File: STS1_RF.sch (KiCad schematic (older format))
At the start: 6 parts

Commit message: finished schematic
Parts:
- C13, C14, C15, C16: renamed from C?; footprint (none) -> Capacitor_SMD:C_0805_2012Metric
- gave numbers to parts that had none: 2
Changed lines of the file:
@@
 $EndDescr
 $Comp
-L STS1_COBC_RFM:LoRa126XF30 RF?
+L STS1_COBC_RFM:LoRa126XF30 RF1
 U 1 1 612D3FCA
 P 3850 3450
-F 0 "RF?" H 3850 4025 50  0000 C CNN
+F 0 "RF1" H 3850 4025 50  0000 C CNN
 F 1 "LoRa1268F30" H 3850 3934 50  0000 C CNN
 F 2 "" H 3850 3900 50  0001 C CNN
@@
 $EndComp
 $Comp
-L STS1_COBC_RFM:RF4463F30 RF?
+L STS1_COBC_RFM:RF4463F30 RF2
 U 1 1 612D4F50
 P 8200 3600
-F 0 "RF?" H 8200 4225 50  0000 C CNN
+F 0 "RF2" H 8200 4225 50  0000 C CNN
 F 1 "RF4463F30" H 8200 4134 50  0000 C CNN
 F 2 "" H 8200 4100 50  0001 C CNN
@@
 LoRa_VCC
 $Comp
-L power:GND #PWR?
+L power:GND #PWR0147
 U 1 1 612D692F
 P 3300 3200
-F 0 "#PWR?" H 3300 2950 50  0001 C CNN
+F 0 "#PWR0147" H 3300 2950 50  0001 C CNN
 F 1 "GND" V 3305 3072 50  0000 R CNN
 F 2 "" H 3300 3200 50  0001 C CNN
@@
 $EndComp
 $Comp
-L power:GND #PWR?
+L power:GND #PWR0148
 U 1 1 612D703E
 P 3300 3800
-F 0 "#PWR?" H 3300 3550 50  0001 C CNN
+F 0 "#PWR0148" H 3300 3550 50  0001 C CNN
 F 1 "GND" V 3305 3672 50  0000 R CNN
 F 2 "" H 3300 3800 50  0001 C CNN
@@
 	2550 3100 2650 3100
 $Comp
-L Device:C C?
+L Device:C C14
 U 1 1 612D80B3
 P 2900 3350
-F 0 "C?" H 3015 3396 50  0000 L CNN
+F 0 "C14" H 3015 3396 50  0000 L CNN
 F 1 "47u" H 3015 3305 50  0000 L CNN
-F 2 "" H 2938 3200 50  0001 C CNN
+F 2 "Capacitor_SMD:C_0805_2012Metric" H 2938 3200 50  0001 C CNN
 F 3 "~" H 2900 3350 50  0001 C CNN
 	1    2900 3350
@@
 $EndComp
 $Comp
-L Device:C C?
+L Device:C C13
 U 1 1 612D8225
 P 2650 3350
-F 0 "C?" H 2450 3450 50  0000 L CNN
+F 0 "C13" H 2450 3450 50  0000 L CNN
 F 1 "100n" H 2500 3350 50  0000 L CNN
-F 2 "" H 2688 3200 50  0001 C CNN
+F 2 "Capacitor_SMD:C_0805_2012Metric" H 2688 3200 50  0001 C CNN
 F 3 "~" H 2650 3350 50  0001 C CNN
 	1    2650 3350
@@
 $EndComp
 $Comp
-L power:GND #PWR?
+L power:GND #PWR0149
 U 1 1 612D8F9E
 P 2650 3500
-F 0 "#PWR?" H 2650 3250 50  0001 C CNN
+F 0 "#PWR0149" H 2650 3250 50  0001 C CNN
 F 1 "GND" H 2655 3327 50  0000 C CNN
 F 2 "" H 2650 3500 50  0001 C CNN
@@
 $EndComp
 $Comp
-L power:GND #PWR?
+L power:GND #PWR0150
 U 1 1 612D9513
 P 2900 3500
-F 0 "#PWR?" H 2900 3250 50  0001 C CNN
+F 0 "#PWR0150" H 2900 3250 50  0001 C CNN
 F 1 "GND" H 2905 3327 50  0000 C CNN
 F 2 "" H 2900 3500 50  0001 C CNN
@@
 	2900 3100 3300 3100
 $Comp
-L power:GND #PWR?
+L power:GND #PWR0151
 U 1 1 612D987F
 P 3300 3500
-F 0 "#PWR?" H 3300 3250 50  0001 C CNN
+F 0 "#PWR0151" H 3300 3250 50  0001 C CNN
 F 1 "GND" V 3305 3372 50  0000 R CNN
 F 2 "" H 3300 3500 50  0001 C CNN
@@
 RF4463_VCC
 $Comp
-L power:GND #PWR?
+L power:GND #PWR0152
 U 1 1 612DA405
 P 7650 3300
-F 0 "#PWR?" H 7650 3050 50  0001 C CNN
+F 0 "#PWR0152" H 7650 3050 50  0001 C CNN
 F 1 "GND" V 7655 3172 50  0000 R CNN
 F 2 "" H 7650 3300 50  0001 C CNN
@@
 $EndComp
 $Comp
-L power:GND #PWR?
+L power:GND #PWR0153
 U 1 1 612DA9D3
 P 7650 3600
-F 0 "#PWR?" H 7650 3350 50  0001 C CNN
+F 0 "#PWR0153" H 7650 3350 50  0001 C CNN
 F 1 "GND" V 7655 3472 50  0000 R CNN
 F 2 "" H 7650 3600 50  0001 C CNN
@@
 $EndComp
 $Comp
-L power:GND #PWR?
+L power:GND #PWR0154
 U 1 1 612DAECB
 P 7650 3900
-F 0 "#PWR?" H 7650 3650 50  0001 C CNN
+F 0 "#PWR0154" H 7650 3650 50  0001 C CNN
 F 1 "GND" V 7655 3772 50  0000 R CNN
 F 2 "" H 7650 3900 50  0001 C CNN
@@
 RF4463_ANT
 $Comp
-L Device:C C?
+L Device:C C16
 U 1 1 612DB4E1
 P 7250 3350
-F 0 "C?" H 7200 3350 50  0000 L CNN
+F 0 "C16" H 7200 3350 50  0000 L CNN
 F 1 "47u" H 7200 3250 50  0000 L CNN
-F 2 "" H 7288 3200 50  0001 C CNN
+F 2 "Capacitor_SMD:C_0805_2012Metric" H 7288 3200 50  0001 C CNN
 F 3 "~" H 7250 3350 50  0001 C CNN
 	1    7250 3350
@@
 	7250 3200 7650 3200
 $Comp
-L Device:C C?
+L Device:C C15
 U 1 1 612DBAA7
 P 7000 3350
-F 0 "C?" H 6900 3350 50  0000 L CNN
+F 0 "C15" H 6900 3350 50  0000 L CNN
 F 1 "100n" H 6950 3250 50  0000 L CNN
-F 2 "" H 7038 3200 50  0001 C CNN
+F 2 "Capacitor_SMD:C_0805_2012Metric" H 7038 3200 50  0001 C CNN
 F 3 "~" H 7000 3350 50  0001 C CNN
 	1    7000 3350
@@
 $EndComp
 $Comp
-L power:GND #PWR?
+L power:GND #PWR0155
 U 1 1 612DBF97
 P 7000 3500
-F 0 "#PWR?" H 7000 3250 50  0001 C CNN
+F 0 "#PWR0155" H 7000 3250 50  0001 C CNN
 F 1 "GND" H 7005 3327 50  0000 C CNN
 F 2 "" H 7000 3500 50  0001 C CNN
@@
 $EndComp
 $Comp
-L power:GND #PWR?
+L power:GND #PWR0156
 U 1 1 612DC2BC
 P 7250 3500
-F 0 "#PWR?" H 7250 3250 50  0001 C CNN
+F 0 "#PWR0156" H 7250 3250 50  0001 C CNN
 F 1 "GND" H 7255 3327 50  0000 C CNN
 F 2 "" H 7250 3500 50  0001 C CNN

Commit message: schematic done
final tweaks (adding LEDS, pin headers, moving circuits...)
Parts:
- added D5: LED, symbol Device:LED
- added J39, J40: Conn_Coaxial, symbol Connector:Conn_Coaxial
- added JP3, JP4, JP? (x2): Jumper_NC_Dual, symbol Device:Jumper_NC_Dual
- added R13: 15, symbol Device:R
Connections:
- net GND: now also JP3.1, JP4.1, JP?.3, JP?.3, R13.2; no longer RF1.5 (NRESET), RF2.5 (SDN)
- net LoRa_SMA_GND: now also J39.2 (Ext)
- net LoRa_VCC: now also JP3.3, JP?.1, JP?.1
- net RF4463_ANT_GND: now also J40.2 (Ext)
- net RF4463_VCC: now also JP4.3
- net at RF1.13 (DIO1): now also JP?.2
- net at RF1.14 (DIO3): now also JP?.2
- net at RF1.6 (BUSY): now also D5.2 (A)
- net LoRa_ANT: no longer names the net of RF1.16 (ANT)
- net LoRa_ANT: now also J39.1 (In)
- net RF4463_ANT: no longer names the net of RF2.16 (ANT)
- net RF4463_ANT: now also J40.1 (In)
- new net: JP3.2, RF1.5 (NRESET)
- new net: JP4.2, RF2.5 (SDN)
- new net: D5.1 (K), R13.1
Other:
- note added: "Blaue LED\n3V typ / 20mA typ"
- note added: "Busy pin und DIO pins (customizable digital I/O pins)\nWhen busy is high the host controller must wait to till the busy line is low to send another command\n"
- note added: "In LAYOUT, the GND (pin 15) next to the ANT (pin 16) pin cannot be directly connected to the \nground of the system. It can be connected to the GND of the external SMA socket\n\nEvtl LED an GPIOs hängen(OK von Peter)\n"
- note removed: "Busy pin und DIO pins ?\n"
- note removed: "In LAYOUT, the GND (pin 15) next to the ANT (pin 16) pin cannot be directly connected to the \nground of the system. It can be connected to the GND of the external SMA socket"
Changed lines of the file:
@@
 $Descr A4 11693 8268
 encoding utf-8
-Sheet 7 7
+Sheet 4 5
 Title ""
 Date ""
@@
 	0    1    1    0
 $EndComp
-Text HLabel 4400 3200 2    50   Input ~ 0
+Text HLabel 4650 3200 2    50   Input ~ 0
 LoRa_SMA_GND
-Text Notes 5900 2800 2    50   ~ 0
- In LAYOUT, the GND (pin 15) next to the ANT (pin 16) pin cannot be directly connected to the \nground of the system. It can be connected to the GND of the external SMA socket
+Text Notes 7300 2250 2    50   ~ 0
+ In LAYOUT, the GND (pin 15) next to the ANT (pin 16) pin cannot be directly connected to the \nground of the system. It can be connected to the GND of the external SMA socket\n\nEvtl LED an GPIOs hängen(OK von Peter)\n
 Wire Wire Line
 	2550 3100 2650 3100
@@
 L power:GND #PWR0151
 U 1 1 612D987F
-P 3300 3500
-F 0 "#PWR0151" H 3300 3250 50  0001 C CNN
-F 1 "GND" V 3305 3372 50  0000 R CNN
-F 2 "" H 3300 3500 50  0001 C CNN
-F 3 "" H 3300 3500 50  0001 C CNN
-	1    3300 3500
-	0    1    1    0
+P 1850 4000
+F 0 "#PWR0151" H 1850 3750 50  0001 C CNN
+F 1 "GND" V 1855 3872 50  0000 R CNN
+F 2 "" H 1850 4000 50  0001 C CNN
+F 3 "" H 1850 4000 50  0001 C CNN
+	1    1850 4000
+	1    0    0    -1
 $EndComp
 Text HLabel 4400 3800 2    50   Input ~ 0
@@
 LoRa_NSS
 Text Notes 3600 2550 0    50   ~ 0
-Busy pin und DIO pins ?\n
+Busy pin und DIO pins  (customizable digital I/O pins)\nWhen busy is high the host controller must wait to till the busy line is low to send another command\n
 Text HLabel 6900 3200 0    50   Input ~ 0
 RF4463_VCC
@@
 L power:GND #PWR0153
 U 1 1 612DA9D3
-P 7650 3600
-F 0 "#PWR0153" H 7650 3350 50  0001 C CNN
-F 1 "GND" V 7655 3472 50  0000 R CNN
-F 2 "" H 7650 3600 50  0001 C CNN
-F 3 "" H 7650 3600 50  0001 C CNN
-	1    7650 3600
-	0    1    1    0
+P 6350 4200
+F 0 "#PWR0153" H 6350 3950 50  0001 C CNN
+F 1 "GND" V 6355 4072 50  0000 R CNN
+F 2 "" H 6350 4200 50  0001 C CNN
+F 3 "" H 6350 4200 50  0001 C CNN
+	1    6350 4200
+	1    0    0    -1
 $EndComp
 $Comp
@@
 	0    1    1    0
 $EndComp
-Text HLabel 8750 3300 2    50   Input ~ 0
+Text HLabel 9000 3300 2    50   Input ~ 0
 RF4463_ANT_GND
-Text HLabel 8750 3200 2    50   Input ~ 0
-RF4463_ANT
 $Comp
 L Device:C C16
@@
 Text HLabel 8750 3900 2    50   Input ~ 0
 RF4463_SPI_CLK
-Text HLabel 4400 3100 2    50   Input ~ 0
-LoRa_ANT
+$Comp
+L Connector:Conn_Coaxial J39
+U 1 1 616A0FD1
+P 4650 3000
+F 0 "J39" H 4750 2975 50  0000 L CNN
+F 1 "Conn_Coaxial" H 4750 2884 50  0000 L CNN
+F 2 "" H 4650 3000 50  0001 C CNN
+F 3 " ~" H 4650 3000 50  0001 C CNN
+	1    4650 3000
+	1    0    0    -1
+$EndComp
+Wire Wire Line
+	4400 3100 4450 3100
+Wire Wire Line
+	4450 3100 4450 3000
+Wire Wire Line
+	4650 3200 4400 3200
+$Comp
+L Connector:Conn_Coaxial J40
+U 1 1 616A364E
+P 9000 3050
+F 0 "J40" H 9100 3025 50  0000 L CNN
+F 1 "Conn_Coaxial" H 9100 2934 50  0000 L CNN
+F 2 "" H 9000 3050 50  0001 C CNN
+F 3 " ~" H 9000 3050 50  0001 C CNN
+	1    9000 3050
+	1    0    0    -1
+$EndComp
+Wire Wire Line
+	8800 3050 8800 3200
+Wire Wire Line
+	8800 3200 8750 3200
+Wire Wire Line
+	8750 3300 9000 3300
+Wire Wire Line
+	9000 3300 9000 3250
+$Comp
+L Device:LED D5
+U 1 1 616A59D7
+P 3000 4100
+F 0 "D5" V 3039 3982 50  0000 R CNN
+F 1 "LED" V 2948 3982 50  0000 R CNN
+F 2 "" H 3000 4100 50  0001 C CNN
+F 3 "~" H 3000 4100 50  0001 C CNN
+	1    3000 4100
+	0    -1   -1   0
+$EndComp
+Wire Wire Line
+	3300 3600 3000 3600
+$Comp
+L Device:R R13
+U 1 1 616A6F08
+P 3000 4500
+F 0 "R13" H 3070 4546 50  0000 L CNN
+F 1 "15" H 3070 4455 50  0000 L CNN
+F 2 "" V 2930 4500 50  0001 C CNN
+F 3 "~" H 3000 4500 50  0001 C CNN
+	1    3000 4500
+	1    0    0    -1
+$EndComp
+Wire Wire Line
+	3000 4250 3000 4350
+$Comp
+L power:GND #PWR0173
+U 1 1 616A7A03
+P 3000 4800
+F 0 "#PWR0173" H 3000 4550 50  0001 C CNN
+F 1 "GND" V 3005 4672 50  0000 R CNN
+F 2 "" H 3000 4800 50  0001 C CNN
+F 3 "" H 3000 4800 50  0001 C CNN
+	1    3000 4800
+	1    0    0    -1
+$EndComp
+Wire Wire Line
+	3000 4650 3000 4800
+Text Notes 3250 4500 0    50   ~ 0
+Blaue LED\n3V typ / 20mA typ
+$Comp
+L Device:Jumper_NC_Dual JP3
+U 1 1 616A9A84
+P 1850 3750
+F 0 "JP3" V 1896 3852 50  0000 L CNN
+F 1 "Jumper_NC_Dual" V 1805 3852 50  0000 L CNN
+F 2 "" H 1850 3750 50  0001 C CNN
+F 3 "~" H 1850 3750 50  0001 C CNN
+	1    1850 3750
+	0    -1   -1   0
+$EndComp
+Wire Wire Line
+	3000 3600 3000 3950
+Wire Wire Line
+	2100 3500 2100 3750
+Wire Wire Line
+	2100 3750 1950 3750
+Wire Wire Line
+	2100 3500 3300 3500
+Wire Wire Line
+	2650 3100 2650 2950
+Wire Wire Line
+	2650 2950 1850 2950
+Wire Wire Line
+	1850 2950 1850 3500
+$Comp
+L Device:Jumper_NC_Dual JP4
+U 1 1 616ADAD3
+P 6350 3950
+F 0 "JP4" V 6396 4052 50  0000 L CNN
+F 1 "Jumper_NC_Dual" V 6305 4052 50  0000 L CNN
+F 2 "" H 6350 3950 50  0001 C CNN
+F 3 "~" H 6350 3950 50  0001 C CNN
+	1    6350 3950
+	0    -1   -1   0
+$EndComp
+Wire Wire Line
+	7650 3600 7300 3600
+Wire Wire Line
+	7300 3600 7300 3950
+Wire Wire Line
+	7300 3950 6450 3950
+Wire Wire Line
+	6350 3700 6350 2950
+Wire Wire Line
+	6350 2950 7000 2950
+Wire Wire Line
+	7000 2950 7000 3200
+$Comp
+L Device:Jumper_NC_Dual JP?
+U 1 1 6168BA24
+P 5550 3300
+F 0 "JP?" V 5596 3402 50  0000 L CNN
+F 1 "Jumper_NC_Dual" V 5505 3402 50  0000 L CNN
+F 2 "" H 5550 3300 50  0001 C CNN
+F 3 "~" H 5550 3300 50  0001 C CNN
+	1    5550 3300
+	0    1    1    0
+$EndComp
+$Comp
+L power:GND #PWR?
+U 1 1 6168C756
+P 5550 3550
+F 0 "#PWR?" H 5550 3300 50  0001 C CNN
+F 1 "GND" V 5555 3422 50  0000 R CNN
+F 2 "" H 5550 3550 50  0001 C CNN
+F 3 "" H 5550 3550 50  0001 C CNN
+	1    5550 3550
+	1    0    0    -1
+$EndComp
+Wire Wire Line
+	5550 3050 5550 2800
+Wire Wire Line
+	5550 2800 5300 2800
+Wire Wire Line
+	2900 2800 2900 3100
+Wire Wire Line
+	4400 3300 5450 3300
+$Comp
+L Device:Jumper_NC_Dual JP?
+U 1 1 6168DEC2
+P 5300 4150
+F 0 "JP?" V 5346 4252 50  0000 L CNN
+F 1 "Jumper_NC_Dual" V 5255 4252 50  0000 L CNN
+F 2 "" H 5300 4150 50  0001 C CNN
+F 3 "~" H 5300 4150 50  0001 C CNN
+	1    5300 4150
+	0    1    1    0
+$EndComp
+$Comp
+L power:GND #PWR?
+U 1 1 6168E6D9
+P 5300 4400
+F 0 "#PWR?" H 5300 4150 50  0001 C CNN
+F 1 "GND" V 5305 4272 50  0000 R CNN
+F 2 "" H 5300 4400 50  0001 C CNN
+F 3 "" H 5300 4400 50  0001 C CNN
+	1    5300 4400
+	1    0    0    -1
+$EndComp
+Wire Wire Line
+	5200 4150 5150 4150
+Wire Wire Line
+	5150 4150 5150 3400
+Wire Wire Line
+	5150 3400 4400 3400
+Wire Wire Line
+	5300 3900 5300 2800
+Connection ~ 5300 2800
+Wire Wire Line
+	5300 2800 2900 2800
 $EndSCHEMATC

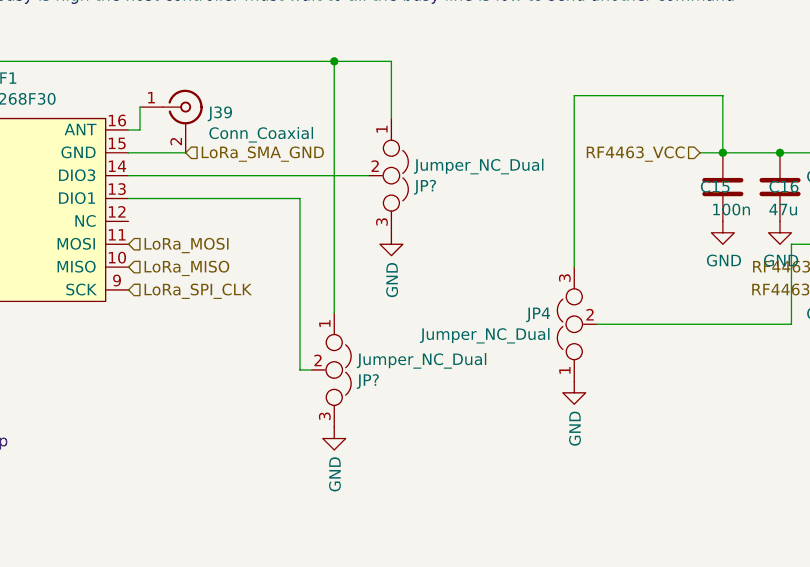
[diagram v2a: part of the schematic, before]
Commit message: Issues removed + further layout development
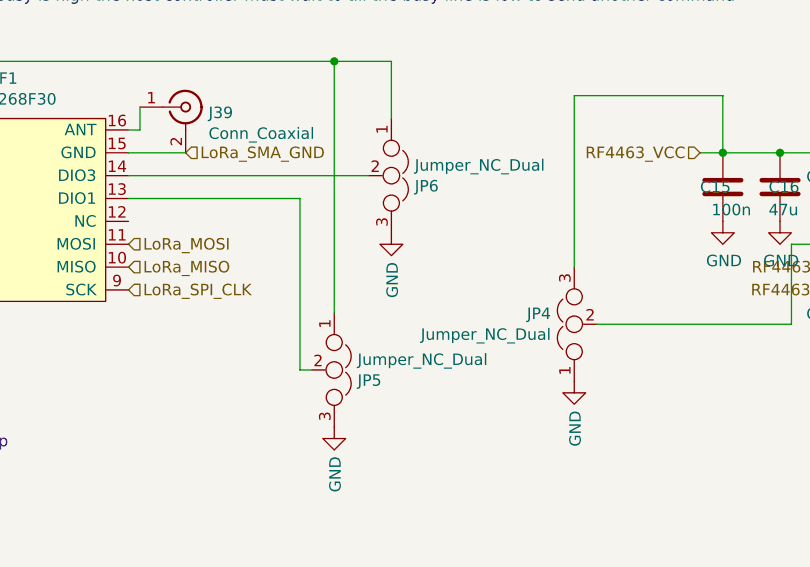
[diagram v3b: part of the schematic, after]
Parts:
- D5: footprint (none) -> LED_SMD:LED_0805_2012Metric
- JP3, JP4: footprint (none) -> Connector_PinHeader_2.54mm:PinHeader_1x03_P2.54mm_Vertical
- JP5, JP6: renamed from JP?; footprint (none) -> Connector_PinHeader_2.54mm:PinHeader_1x03_P2.54mm_Vertical
- R13: footprint (none) -> Resistor_SMD:R_0805_2012Metric
- RF1: footprint (none) -> STS1_RF:LoRa1268F30
- RF2: footprint (none) -> STS1_RF:STS1_RF4463F30
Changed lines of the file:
@@
 $Descr A4 11693 8268
 encoding utf-8
-Sheet 4 5
+Sheet 3 5
 Title ""
 Date ""
@@
 F 0 "RF1" H 3850 4025 50  0000 C CNN
 F 1 "LoRa1268F30" H 3850 3934 50  0000 C CNN
-F 2 "" H 3850 3900 50  0001 C CNN
+F 2 "STS1_RF:LoRa1268F30" H 3850 3900 50  0001 C CNN
 F 3 "" H 3850 3900 50  0001 C CNN
 	1    3850 3450
@@
 F 0 "RF2" H 8200 4225 50  0000 C CNN
 F 1 "RF4463F30" H 8200 4134 50  0000 C CNN
-F 2 "" H 8200 4100 50  0001 C CNN
+F 2 "STS1_RF:STS1_RF4463F30" H 8200 4100 50  0001 C CNN
 F 3 "" H 8200 4100 50  0001 C CNN
 	1    8200 3600
@@
 F 0 "D5" V 3039 3982 50  0000 R CNN
 F 1 "LED" V 2948 3982 50  0000 R CNN
-F 2 "" H 3000 4100 50  0001 C CNN
+F 2 "LED_SMD:LED_0805_2012Metric" H 3000 4100 50  0001 C CNN
 F 3 "~" H 3000 4100 50  0001 C CNN
 	1    3000 4100
@@
 F 0 "R13" H 3070 4546 50  0000 L CNN
 F 1 "15" H 3070 4455 50  0000 L CNN
-F 2 "" V 2930 4500 50  0001 C CNN
+F 2 "Resistor_SMD:R_0805_2012Metric" V 2930 4500 50  0001 C CNN
 F 3 "~" H 3000 4500 50  0001 C CNN
 	1    3000 4500
@@
 F 0 "JP3" V 1896 3852 50  0000 L CNN
 F 1 "Jumper_NC_Dual" V 1805 3852 50  0000 L CNN
-F 2 "" H 1850 3750 50  0001 C CNN
+F 2 "Connector_PinHeader_2.54mm:PinHeader_1x03_P2.54mm_Vertical" H 1850 3750 50  0001 C CNN
 F 3 "~" H 1850 3750 50  0001 C CNN
 	1    1850 3750
@@
 F 0 "JP4" V 6396 4052 50  0000 L CNN
 F 1 "Jumper_NC_Dual" V 6305 4052 50  0000 L CNN
-F 2 "" H 6350 3950 50  0001 C CNN
+F 2 "Connector_PinHeader_2.54mm:PinHeader_1x03_P2.54mm_Vertical" H 6350 3950 50  0001 C CNN
 F 3 "~" H 6350 3950 50  0001 C CNN
 	1    6350 3950
@@
 	7000 2950 7000 3200
 $Comp
-L Device:Jumper_NC_Dual JP?
+L Device:Jumper_NC_Dual JP6
 U 1 1 6168BA24
 P 5550 3300
-F 0 "JP?" V 5596 3402 50  0000 L CNN
+F 0 "JP6" V 5596 3402 50  0000 L CNN
 F 1 "Jumper_NC_Dual" V 5505 3402 50  0000 L CNN
-F 2 "" H 5550 3300 50  0001 C CNN
+F 2 "Connector_PinHeader_2.54mm:PinHeader_1x03_P2.54mm_Vertical" H 5550 3300 50  0001 C CNN
 F 3 "~" H 5550 3300 50  0001 C CNN
 	1    5550 3300
@@
 $EndComp
 $Comp
-L power:GND #PWR?
+L power:GND #PWR0110
 U 1 1 6168C756
 P 5550 3550
-F 0 "#PWR?" H 5550 3300 50  0001 C CNN
+F 0 "#PWR0110" H 5550 3300 50  0001 C CNN
 F 1 "GND" V 5555 3422 50  0000 R CNN
 F 2 "" H 5550 3550 50  0001 C CNN
@@
 	4400 3300 5450 3300
 $Comp
-L Device:Jumper_NC_Dual JP?
+L Device:Jumper_NC_Dual JP5
 U 1 1 6168DEC2
 P 5300 4150
-F 0 "JP?" V 5346 4252 50  0000 L CNN
+F 0 "JP5" V 5346 4252 50  0000 L CNN
 F 1 "Jumper_NC_Dual" V 5255 4252 50  0000 L CNN
-F 2 "" H 5300 4150 50  0001 C CNN
+F 2 "Connector_PinHeader_2.54mm:PinHeader_1x03_P2.54mm_Vertical" H 5300 4150 50  0001 C CNN
 F 3 "~" H 5300 4150 50  0001 C CNN
 	1    5300 4150
@@
 $EndComp
 $Comp
-L power:GND #PWR?
+L power:GND #PWR0111
 U 1 1 6168E6D9
 P 5300 4400
-F 0 "#PWR?" H 5300 4150 50  0001 C CNN
+F 0 "#PWR0111" H 5300 4150 50  0001 C CNN
 F 1 "GND" V 5305 4272 50  0000 R CNN
 F 2 "" H 5300 4400 50  0001 C CNN

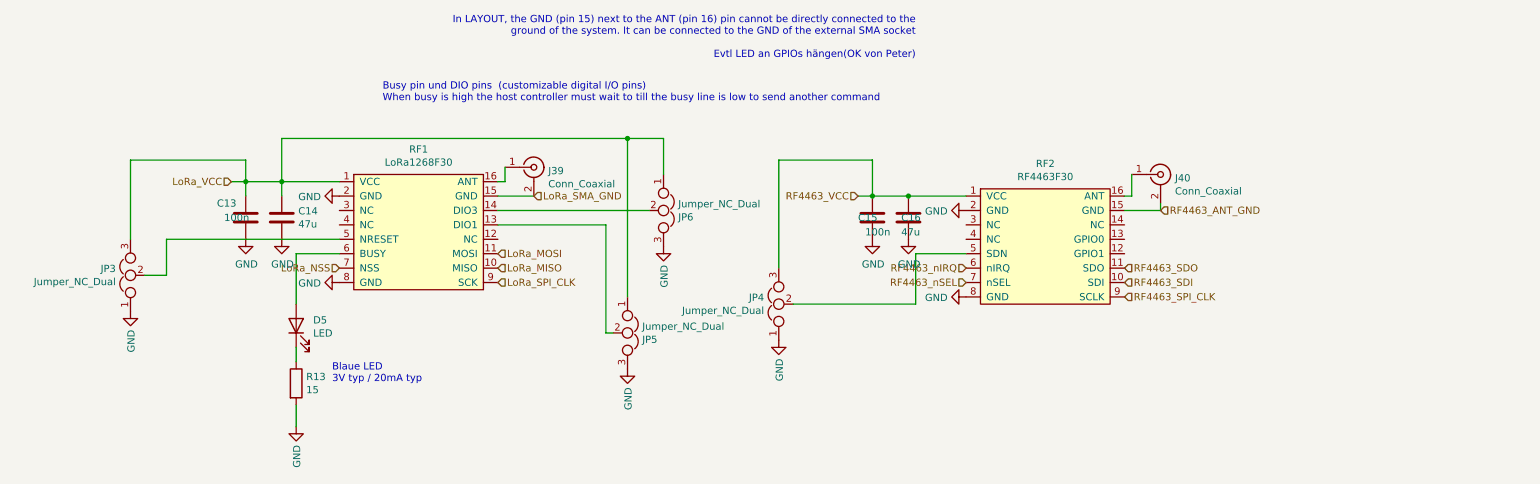
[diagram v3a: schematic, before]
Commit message: component layout finished -> now wiring
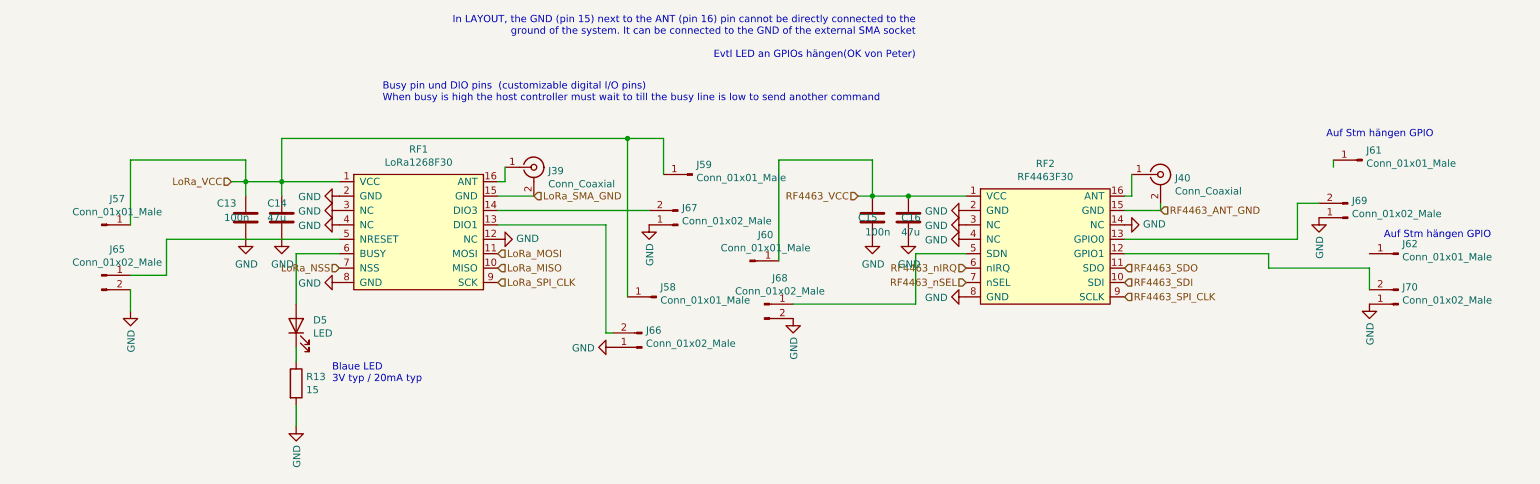
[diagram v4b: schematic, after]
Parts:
- removed JP3, JP4, JP5, JP6: Jumper_NC_Dual, Connector_PinHeader_2.54mm:PinHeader_1x03_P2.54mm_Vertical, symbol Device:Jumper_NC_Dual
- added J57, J58, J59, J60, J61, J62: Conn_01x01_Male, Connector_PinHeader_2.54mm:PinHeader_1x01_P2.54mm_Vertical, symbol Connector:Conn_01x01_Male
- added J65, J66, J67, J68, J69, J70: Conn_01x02_Male, Connector_PinHeader_2.54mm:PinHeader_1x02_P2.54mm_Vertical, symbol Connector:Conn_01x02_Male
- J39, J40: footprint (none) -> Connector_Coaxial:SMA_Amphenol_901-144_Vertical
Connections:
- net GND: now also RF1.12 (NC), RF1.3 (NC), RF1.4 (NC), RF2.14 (NC), RF2.3 (NC), RF2.4 (NC), J65.2 (Pin_2), J66.1 (Pin_1), J67.1 (Pin_1), J68.2 (Pin_2), J69.1 (Pin_1), J70.1 (Pin_1)
- net LoRa_VCC: now also J57.1 (Pin_1), J58.1 (Pin_1), J59.1 (Pin_1)
- net RF4463_VCC: now also J60.1 (Pin_1)
- net at RF1.13 (DIO1): now also J66.2 (Pin_2)
- net at RF1.14 (DIO3): now also J67.2 (Pin_2)
- net at RF1.5 (NRESET): now also J65.1 (Pin_1)
- net at RF2.12 (GPIO1): now also J70.2 (Pin_2)
- net at RF2.13 (GPIO0): now also J69.2 (Pin_2)
- net at RF2.5 (SDN): now also J68.1 (Pin_1)
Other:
- note added: "Auf Stm hängen GPIO\n"
